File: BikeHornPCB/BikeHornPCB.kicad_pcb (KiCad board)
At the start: 2 copper layers, 35 x 51 mm, 20 parts, among them J1 Battery, J2 Horn, J3 Piezo, Q1 BC337, Q2 BC337

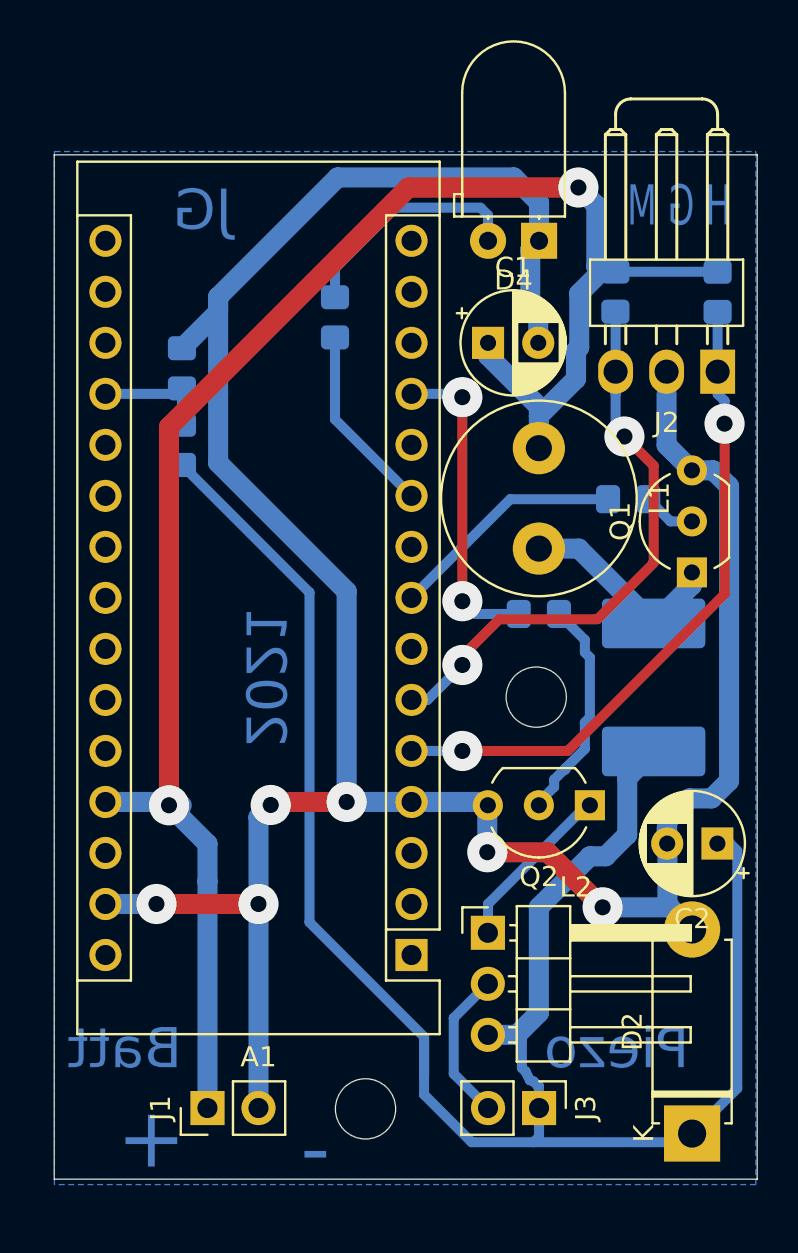
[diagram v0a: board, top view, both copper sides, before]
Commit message: Added docs, runtime logging, revised PCB to fix issues from first version built
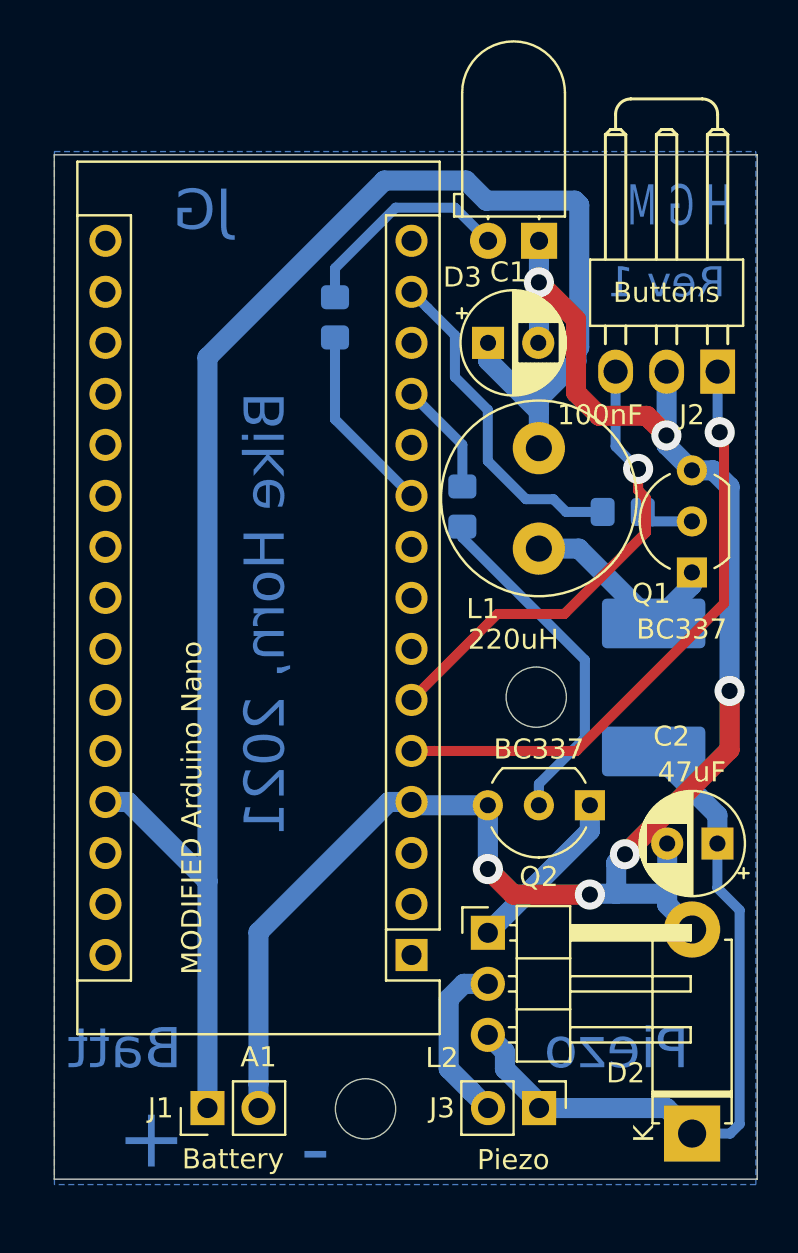
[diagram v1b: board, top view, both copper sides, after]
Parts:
- removed the R3 at (62.2, 45.7)
- removed R4, R5, R6: R, Resistor_SMD:R_0805_2012Metric_Pad1.20x1.40mm_HandSolder
- A1: value Arduino_Nano_v2.x -> MODIFIED Arduino Nano
- C1: value C -> 100nF
- C2: value CP -> 47uF
- D2: value D_Zener -> 22V
- J2: value Horn -> Buttons
- L1: value L -> 220uH
- R1, R2: value 470 -> 180
- R3: renamed from R7; value R -> 249
- moved R2 6.57 mm to (49.5, 56.4), turned to 90 degrees
- moved R1 0.69 mm to (57.5, 56.7)
- renumbered D4 to D3
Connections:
- A1 pad 29: GND -> Net-(A1-Pad29)
- R1 pad 2: Net-(A1-Pad8) -> Net-(A1-Pad14)
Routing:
- net Net-(C2-Pad1): track 93.7 -> 35.7 mm
- net GND: track 137.6 -> 87.8 mm
- net Net-(A1-Pad14): track 0.00 -> 16.8 mm
- net Net-(A1-Pad8): track 11.8 -> 0.00 mm
- net Net-(A1-Pad12): track 16.4 -> 5.66 mm, vias 2 -> 0
- net Net-(Q2-Pad2): track 11.1 -> 17.4 mm
- net Net-(A1-Pad19): track 6.11 -> 0.00 mm
- net +BATT: track 89.1 -> 84.1 mm, vias 2 -> 0
- net Net-(A1-Pad6): track 28.6 -> 23.9 mm, vias 2 -> 1
- net Net-(A1-Pad5): track 33.4 -> 30.3 mm, vias 2 -> 1
- net Net-(J3-Pad2): track 7.60 -> 8.51 mm
- net Net-(D3-Pad2): track 11.7 -> 11.0 mm
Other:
- net class Default: via_dia 2 -> 1.5
- board text added: "Bike Horn, 2021"
- board text added: "Jotham Gates"
- board text added: "Rev 1"
- board text added: "github.com/jgOhYeah/BikeHorn"
- board text removed: "2021"

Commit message: PCD saved for KiCAD 6, added rescue files that should have been there all along
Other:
- net class Default removed
